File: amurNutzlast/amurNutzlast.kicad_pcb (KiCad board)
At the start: 4 copper layers, 126 x 39 mm, 97 parts, among them J1 Conn_01x06, J2 Conn_02x02_Counter_Clockwise, J4 Conn_01x08, J5 Conn_01x07, J6 USB_A, J7 Conn_01x07, J8 Conn_01x20, U1 ICE40HX1K-TQ144, U4 FT2232HL, U5 93LCxxA, U6 W25Q128JVS, U7 LD1117S33TR_SOT223, X1 SG-7050CAN, Y1 Crystal_GND24_Small

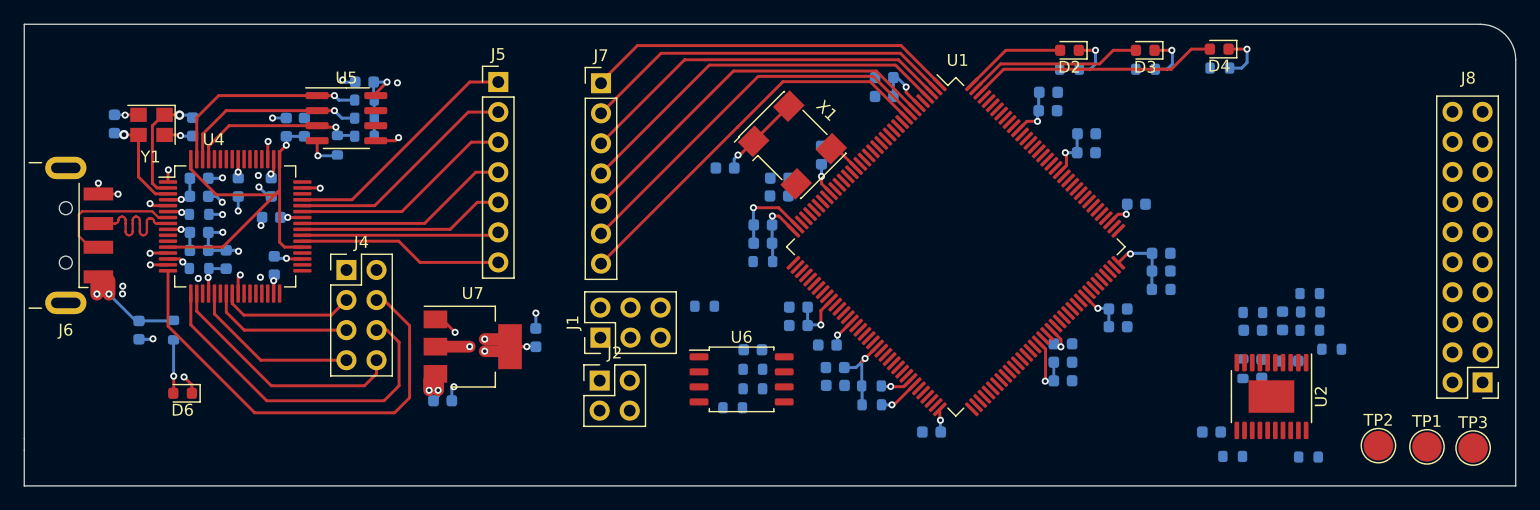
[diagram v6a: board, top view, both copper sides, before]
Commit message: gpio connected
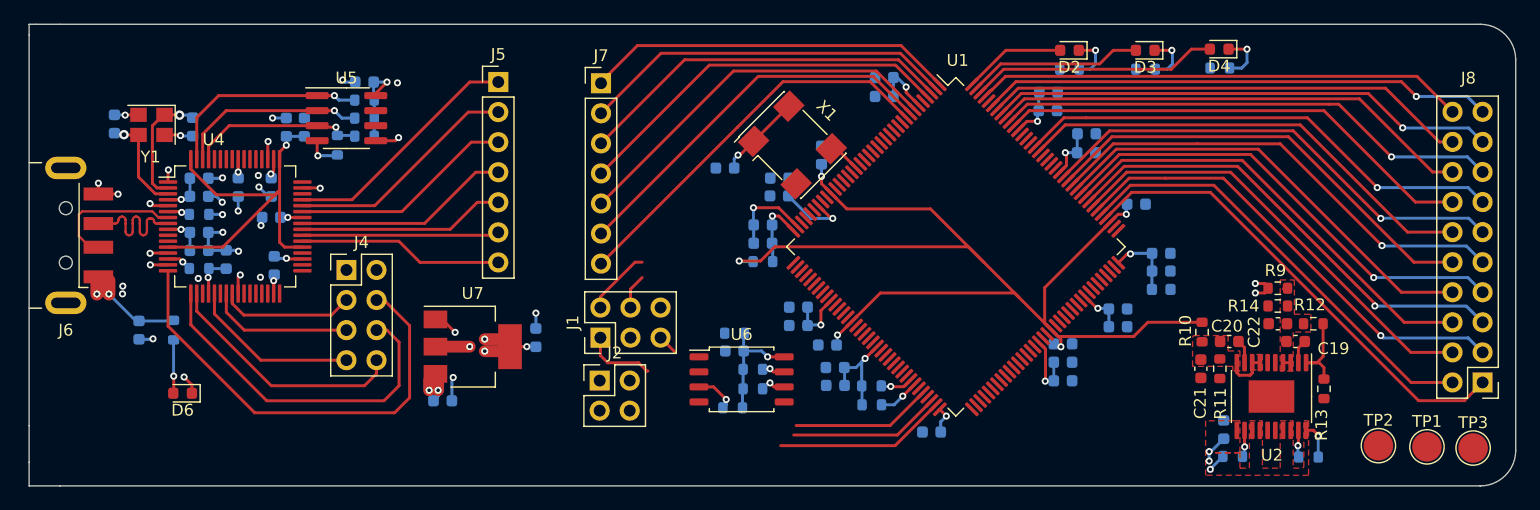
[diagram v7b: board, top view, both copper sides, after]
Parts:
- C19, C20, C21, C22, R10, R11, R12, R13, R14, R9: moved to F.Cu
- moved C21 5.15 mm to (165.4, 112.1)
- moved R10 4.61 mm to (165.5, 109.0), turned to 90 degrees
- moved R13 3.41 mm to (175.8, 113.8), turned to -90 degrees
- moved R15 3.40 mm to (126.0, 109.1)
- moved R14 2.80 mm to (171.9, 106.8), turned to 0 degrees
- moved R9 2.74 mm to (171.9, 105.3), turned to 180 degrees
- moved C20 2.21 mm to (167.8, 109.8), turned to 0 degrees
- moved R11 1.95 mm to (167.0, 112.1)
- moved C19 1.74 mm to (173.4, 109.8)
- moved C24 1.55 mm to (126.0, 110.6)
- moved C23 1.05 mm to (167.3, 117.2), turned to 90 degrees
- moved R12 0.63 mm to (174.9, 108.3)
- moved C22 0.47 mm to (171.9, 108.3), turned to 180 degrees
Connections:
- net Net-(C19-Pad1) renamed /power_management/out_3.3v
- net Net-(U2-ADJ2) renamed /power_management/out_1.2v
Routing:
- net +1V2: track 10.4 -> 97.0 mm, vias 4 -> 5
- net /fpga/PIO19: track 0.00 -> 43.3 mm, vias 0 -> 1
- net /fpga/PIO17: track 0.00 -> 43.1 mm, vias 0 -> 1
- net /fpga/PIO15: track 0.00 -> 43.0 mm, vias 0 -> 1
- net /fpga/PIO13: track 0.00 -> 41.8 mm, vias 0 -> 1
- net /fpga/PIO20: track 0.00 -> 41.5 mm
- net /fpga/PIO18: track 0.00 -> 41.1 mm
- net /fpga/PIO16: track 0.00 -> 41.0 mm
- net /fpga/PIO14: track 0.00 -> 40.8 mm
- net /fpga/PIO1: track 0.00 -> 40.7 mm
- net /fpga/PIO11: track 0.00 -> 40.5 mm, vias 0 -> 1
- net /fpga/PIO9: track 0.00 -> 40.2 mm, vias 0 -> 1
- net /fpga/PIO7: track 0.00 -> 40.1 mm, vias 0 -> 1
- net /fpga/PIO5: track 0.00 -> 40.1 mm, vias 0 -> 1
- net /fpga/PIO3: track 0.00 -> 39.7 mm, vias 0 -> 1
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- added copper zone on In2.Cu, net +3.3V
- added copper zone on F.Cu, net +5V
- added copper zone on In2.Cu, net +5V
- added copper zone on F.Cu, net /power_management/out_1.2v
- added copper zone on F.Cu, net /power_management/out_3.3v
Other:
- board size 126 x 39 mm -> 125.6 x 39 mm

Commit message: finished pcb
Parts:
- removed J4: Conn_01x08, Connector_PinHeader_2.54mm:PinHeader_2x04_P2.54mm_Vertical
- added H1: MountingHole_Pad, MountingHole:MountingHole_2.5mm_Pad_Via, F.Cu at (160.8, 33.3)
- added H2: MountingHole_Pad, MountingHole:MountingHole_2.5mm_Pad_Via, F.Cu at (53.3, 33.3)
- added H3: MountingHole_Pad, MountingHole:MountingHole_2.5mm_Pad_Via, F.Cu at (53.2, 65.8)
- added H5: MountingHole_Pad, MountingHole:MountingHole_2.5mm_Pad_Via, F.Cu at (160.8, 65.7)
- added J3: Conn_01x06, Connector_PinHeader_2.54mm:PinHeader_2x03_P2.54mm_Vertical, F.Cu at (76.9, 53.2)
- moved TP3 79.1 mm to (130.0, 65.5), turned to 90 degrees
- moved TP1 73.0 mm to (134.5, 65.5), turned to 90 degrees
- moved TP2 67.3 mm to (139.0, 65.5), turned to 90 degrees
- moved J8 60.0 mm to (159.8, 61.0)
- moved C23 58.0 mm to (143.3, 64.5)
- moved C19 58.0 mm to (149.3, 57.0)
- moved C20 58.0 mm to (143.7, 57.0)
- moved C22 58.0 mm to (147.8, 55.5)
- moved R10 58.0 mm to (141.4, 56.2)
- moved R12 58.0 mm to (150.8, 55.5)
- moved R13 58.0 mm to (151.7, 61.0)
- moved R14 58.0 mm to (147.8, 54.0)
- moved R7 58.0 mm to (150.4, 66.8)
- moved R8 58.0 mm to (144.0, 66.8)
- moved U2 58.0 mm to (147.3, 61.7)
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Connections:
- J1 pad 1: /ICE_CREST -> /MISO
- J1 pad 3: /MISO -> /SS
- J1 pad 4: /MOSI -> /ICE_CREST
- J1 pad 5: /SCL -> /MOSI
- J1 pad 6: /SS -> /SCL
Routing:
- net GND: track 0.00 -> 87.7 mm, vias 0 -> 33
- net /SS: track 14.5 -> 39.7 mm, vias 0 -> 2
- net /ICE_CDONE: track 8.38 -> 32.4 mm
- net /MOSI: track 2.94 -> 26.2 mm
- net /ICE_CREST: track 9.60 -> 29.8 mm
- net /MISO: track 11.9 -> 31.8 mm
- net /SCL: track 16.8 -> 32.3 mm, vias 1 -> 2
- net /fpga/PIO10: track 38.4 -> 24.5 mm
- net /fpga/PIO11: track 40.5 -> 26.9 mm
- net /fpga/PIO9: track 40.2 -> 26.8 mm
- net /fpga/PIO7: track 40.1 -> 26.7 mm
- net /fpga/PIO12: track 39.6 -> 26.2 mm
- net /fpga/PIO8: track 38.2 -> 24.9 mm
- net /fpga/PIO13: track 41.8 -> 28.8 mm
- net /fpga/PIO6: track 38.0 -> 25.3 mm
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- added copper zone on B.Cu, net GND
- added copper zone on In1.Cu, net GND
- added copper zone on B.Cu, net GND1
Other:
- board size 125.6 x 39 mm -> 114 x 39 mm
- board text added: "1.2V"
- board text added: "112"
- board text added: "113"
- board text added: "114"
- board text added: "115"
- board text added: "116"
- board text added: "117"
- board text added: "118"
- board text added: "119"
- board text added: "120"
- board text added: "121"
- board text added: "122"
- board text added: "128"
- board text added: "129"
- board text added: "134"
- board text added: "135"
- board text added: "136"
- board text added: "137"
- board text added: "138"
- board text added: "139"
- board text added: "141"
- board text added: "142"
- board text added: "143"
- board text added: "144"
- board text added: "3.3V"
- board text added: "CDN"
- board text added: "CDONE"
- board text added: "CLK"
- board text added: "CRS"
- board text added: "CTS"
- board text added: "DCD"
- board text added: "DSR"
- board text added: "DTR"
- board text added: "FPGA 5V"
- board text added: "FPGA GND"
- board text added: "FTDI 5V"
- board text added: "FTDI GND"
- board text added: "GND"
- board text added: "MI"
- board text added: "MO"
- board text added: "POWER"
- board text added: "RSET"
- board text added: "RTS"
- board text added: "RX"
- board text added: "SCL"
- board text added: "SS"
- board text added: "TX"
